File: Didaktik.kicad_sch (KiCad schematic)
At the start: 127 parts, among them J1 Conn_01x04_MountingPin, J2 AVR-ISP-6, J3 Conn_01x03, Q1 2N2222, SW1 SW_Push_45deg, SW10 SW_Push_45deg, SW11 SW_Push_45deg, SW12 SW_Push_45deg, SW13 SW_Push_45deg, SW14 SW_Push_45deg, SW15 SW_Push_45deg, SW16 SW_Push_45deg, SW17 SW_Push_45deg, SW18 SW_Push_45deg, SW19 SW_Push_45deg, SW2 SW_Push_45deg, SW20 SW_Push_45deg, SW21 SW_Push_45deg, SW22 SW_Push_45deg, SW23 SW_Push_45deg, SW24 SW_Push_45deg, SW25 SW_Push_45deg, SW26 SW_Push_45deg, SW27 SW_Push_45deg, SW28 SW_Push_45deg, SW29 SW_Push_45deg, SW3 SW_Push_45deg, SW30 SW_Push_45deg, SW31 SW_Push_45deg, SW31a1 SW_Push_45deg, SW32 SW_Push_45deg, SW32a1 SW_Push_45deg, SW33 SW_Push_45deg, SW33a1 SW_Push_45deg, SW34 SW_Push_45deg, SW34a1 SW_Push_45deg, SW34b1 SW_Push_45deg, SW35 SW_Push_45deg, SW35a1 SW_Push_45deg, SW35b1 SW_Push_45deg, SW35c1 SW_Push_45deg, SW36 SW_Push_45deg, SW36a1 SW_Push_45deg, SW36b1 SW_Push_45deg, SW36c1 SW_Push_45deg, SW37 SW_Push_45deg, SW37a1 SW_Push_45deg, SW37b1 SW_Push_45deg, SW38 SW_Push_45deg, SW38a1 SW_Push_45deg, SW39 SW_Push_45deg, SW39a1 SW_Push_45deg, SW4 SW_Push_45deg, SW40 SW_Push_45deg, SW40a1 SW_Push_45deg, SW41 RotaryEncoder_Switch, SW42 RotaryEncoder_Switch, SW5 SW_Push_45deg, SW6 SW_Push_45deg, SW7 SW_Push_45deg, SW8 SW_Push_45deg, SW9 SW_Push_45deg, U1 ATmega32U4-M, Y1 Crystal_GND24_Small

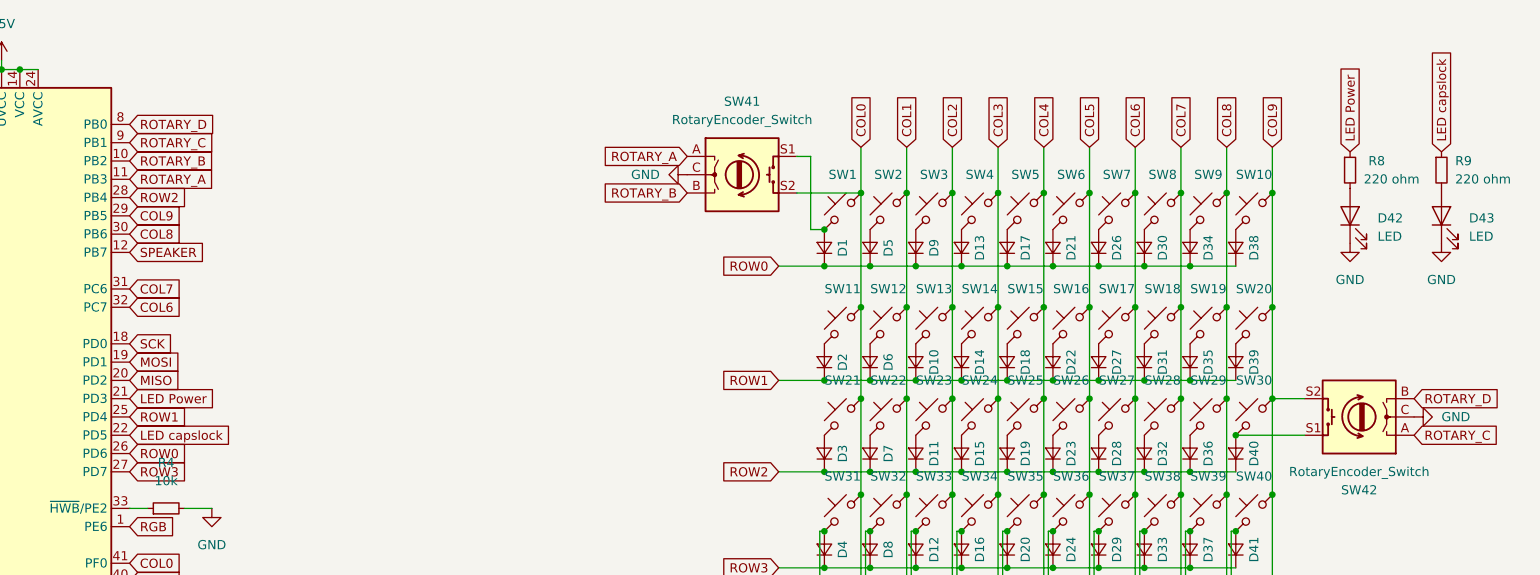
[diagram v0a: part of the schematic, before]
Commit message: clean up folders, created rp2040 version
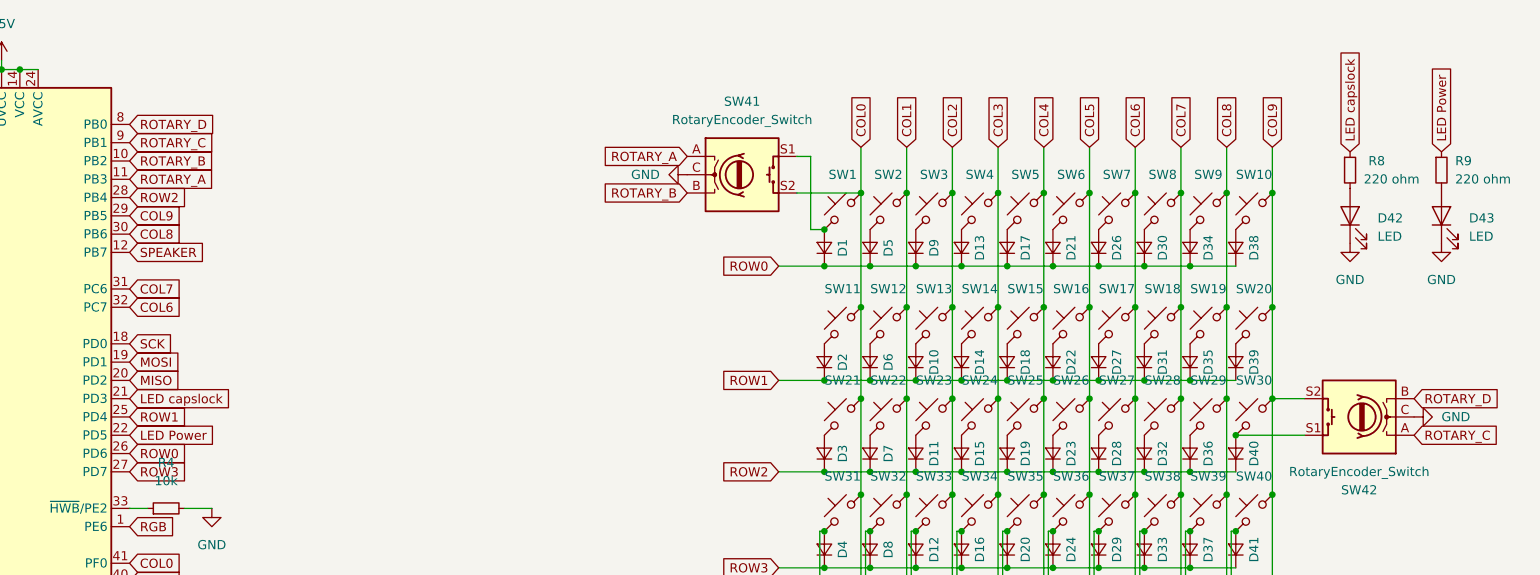
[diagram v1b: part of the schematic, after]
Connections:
- net LED Power: now also R9.1, U1.22 (PD5); no longer R8.1, U1.21 (PD3)
- net LED capslock: now also R8.1, U1.21 (PD3); no longer R9.1, U1.22 (PD5)
